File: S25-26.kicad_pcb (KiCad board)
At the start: 6 copper layers, 90 x 90 mm, 159 parts, among them IC1 CMV4000-3E5M0PN, IC10 DS90LV048ATM_NOPB, IC2 MXL86110I-AQB-R, IC3 TPS5430DDAR, IC4 MT29F2G01ABAGDWB-IT_G_TR, IC5 MT29F2G01ABAGDWB-IT_G_TR, IC6 XMC7200D-E272K8384AA, IC7 DS90LV011AHMF_NOPB, IC8 DS90LV048ATM_NOPB, IC9 DS90LV048ATM_NOPB, J1 DC_IN_PADS, J2 Conn_01x06_Pin, J3 Conn_01x04_Pin, J4 RJ45_JXD1-0001NL, J5 Conn_01x04_Pin, Q1 ZXT849K, U1 TPS73601MDBVREP, U2 TPS73601MDBVREP, Y1 DSC1101DM2-012.0000, Y2 DSC1101DM2-125.0000T

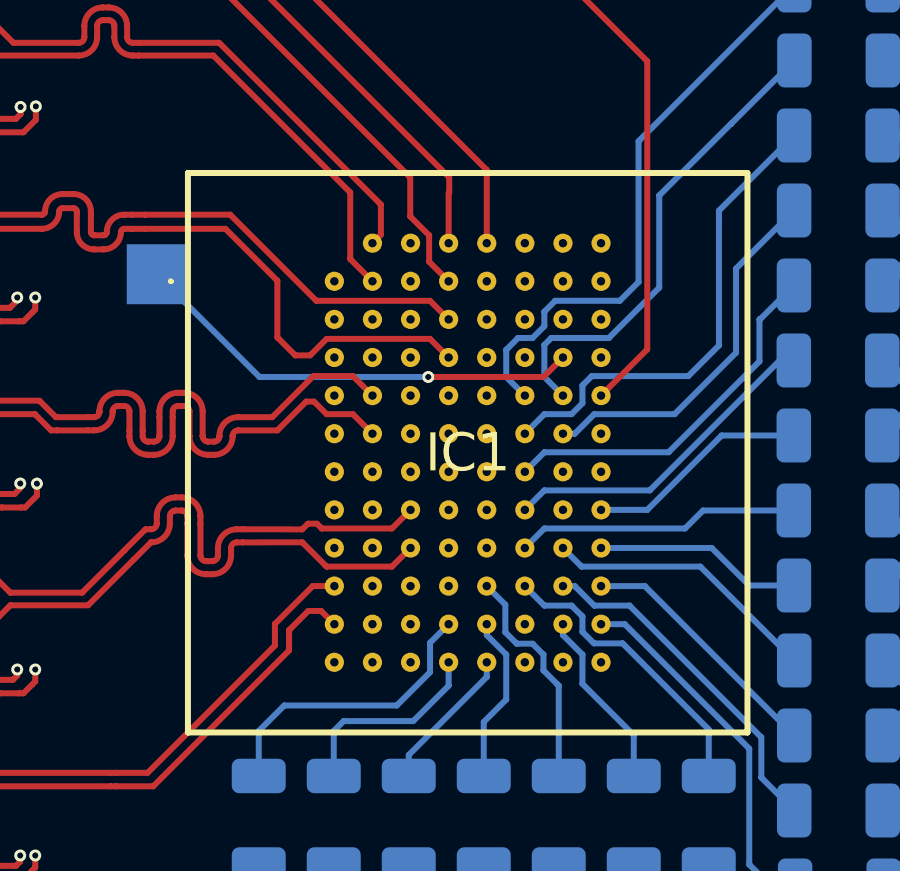
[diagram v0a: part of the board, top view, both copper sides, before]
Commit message: CMOS Sensor Grid Text
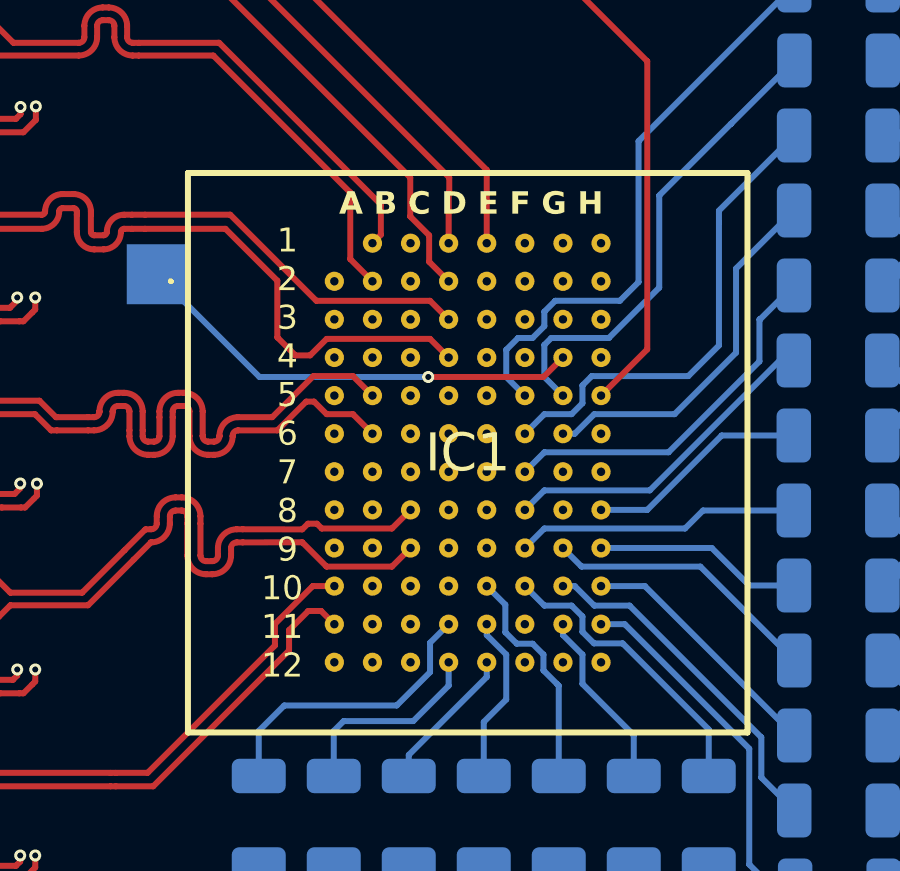
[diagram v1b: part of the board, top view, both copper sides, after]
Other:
- board text added: "1 2 3 4 5 6 7 8 9 10 11 12"
- board text added: "A B C D E F G H"
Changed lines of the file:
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@@
 		(allow_soldermask_bridges_in_footprints no)
 		(tenting front back)
+		(grid_origin 177.5 100)
 		(pcbplotparams
 			(layerselection 0x00000000_00000000_55555555_5755f5ff)
@@
 		)
 	)
+	(gr_text " 1\n 2\n 3\n 4\n 5\n 6\n 7\n 8\n 9\n10\n11\n12"
+		(at 174.23 108.28 0)
+		(layer "F.SilkS")
+		(effects
+			(font
+				(size 0.8 0.8)
+				(thickness 0.15)
+			)
+		)
+	)
 	(gr_text "CTS\n"
 		(at 113.5 106 0)
@@
 			)
 		)
+	)
+	(gr_text "A B C D E F G H"
+		(at 180.53 99.96 0)
+		(layer "F.SilkS")
+		(effects
+			(font
+				(size 0.75 0.75)
+				(thickness 0.15)
+				(bold yes)
+			)
+		)

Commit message: Beginning of V3
Long way to go
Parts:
- added R17: 10k, Resistor_SMD:R_1206_3216Metric, F.Cu at (180.3, 126.3)
- added R18: 10k, Resistor_SMD:R_1206_3216Metric, F.Cu at (180.3, 129.6)
- added R19: 10k, Resistor_SMD:R_1206_3216Metric, F.Cu at (180.3, 132.8)
- IC1: footprint SamacSys_Parts:CMV40003E5M0PN -> CustomFootprintLibrary:CMV40003E5M0PN_Socket
- J2: footprint Connector_PinHeader_2.54mm:PinHeader_1x06_P2.54mm_Vertical -> Connector_PinHeader_1.27mm:PinHeader_2x05_P1.27mm_Vertical_SMD
- J4: footprint Connector_RJ:RJ45_UDE_RB1-125B8G1A -> CustomFootprintLibrary:RJ45_JXD1-0001NL
- Q1: footprint Package_TO_SOT_SMD:TO-252-3_TabPin4 -> CustomFootprintLibrary:TO-252-3_TabPin4
- R6: footprint Resistor_SMD:R_0805_2012Metric -> Resistor_SMD:R_1206_3216Metric
- moved J2 35.3 mm to (186.6, 133.4)
- moved VCORE1 3.48 mm to (169.6, 123.4)
- moved C62 1.45 mm to (171.5, 125.6), turned to 0 degrees
- moved R6 0.71 mm to (166.5, 125.6), turned to 0 degrees
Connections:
- IC6 pad K18: Net-(IC6B-XRES__L) -> /Processing/XRES
- J2 pad 1: /Processing/SWJ_SWCLK_TCLK -> +3V3
- J2 pad 3: /Processing/SWJ_SWO_TDO -> GND
- J2 pad 4: /Processing/SWJ_SWDOE_TDI -> /Processing/SWJ_SWCLK_TCLK
- J2 pad 5: /Processing/SWJ_TRSTN -> GND
- J2 pad 6: GND -> /Processing/SWJ_SWO_TDO
- R14 pad 1: Net-(IC6B-XRES__L) -> /Processing/XRES
- XRES1 pad 1: Net-(IC6B-XRES__L) -> /Processing/XRES
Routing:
- net +3V3: track 566.8 -> 457.7 mm
- net /Processing/SWJ_TRSTN: track 31.5 -> 0.10 mm, vias 2 -> 0
- net Net-(IC6B-XRES__L): track 9.21 -> 0.00 mm, vias 1 -> 0
- net /Processing/XRES: track 0.00 -> 9.21 mm, vias 0 -> 1
- net /Processing/EXT_PS_CTL1: track 80.4 -> 71.5 mm
- added copper zone on F.Cu, net /Processing/EXT_PS_CTL0
- added copper zone on F.Cu, net /Processing/EXT_PS_CTL1

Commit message: Excluded TPs from BOM
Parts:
- removed IC2: MXL86110I-AQB-R, SamacSys_Parts:QFN40P500X500X95-41N-D
- removed R3: 2.49k, Resistor_SMD:R_1206_3216Metric
- removed TP8: VDD1V1, TestPoint:TestPoint_Pad_2.0x2.0mm
- added IC11: DP83867IRPAPT, SamacSys_Parts:QFP50P1200X1200X120-65N, F.Cu at (216.2, 87.0)
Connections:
- net /HRSTN renamed /Processing/HRSTN
- R12 pad 2: Net-(IC2-GPHY_LED0/CFG_EXT) -> unconnected-(R12-Pad2)
- R13 pad 2: Net-(IC2-GPHY_LED1/CFG_LDO0) -> unconnected-(R13-Pad2)
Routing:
- net unconnected-(R12-Pad2): track 0.00 -> 42.0 mm, vias 0 -> 2
- net Net-(IC2-GPHY_LED0/CFG_EXT): track 42.0 -> 0.00 mm, vias 2 -> 0
- net unconnected-(R13-Pad2): track 0.00 -> 37.4 mm, vias 0 -> 2
- net Net-(IC2-GPHY_LED1/CFG_LDO0): track 37.4 -> 0.00 mm, vias 2 -> 0
- net (no net): track 0.00 -> 29.2 mm, vias 0 -> 5
- net /VDD1V1: track 25.4 -> 0.00 mm, vias 5 -> 0
- net Net-(IC2-RCAL): track 3.72 -> 0.00 mm

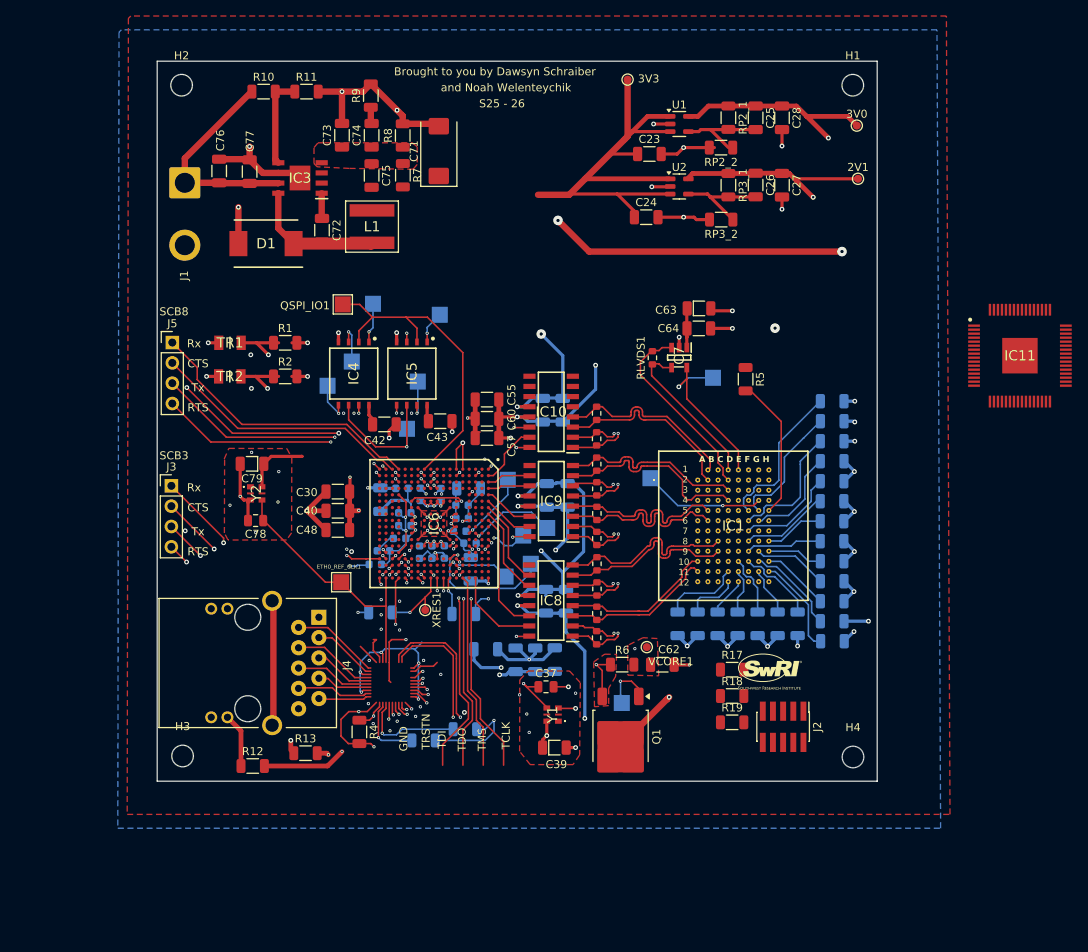
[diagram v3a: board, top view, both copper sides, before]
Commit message: V3 Overhaul
Things remaining:
Ethernet Transceiver Clocks
Output Filtering on DC-DC Converter
Update some part numbers
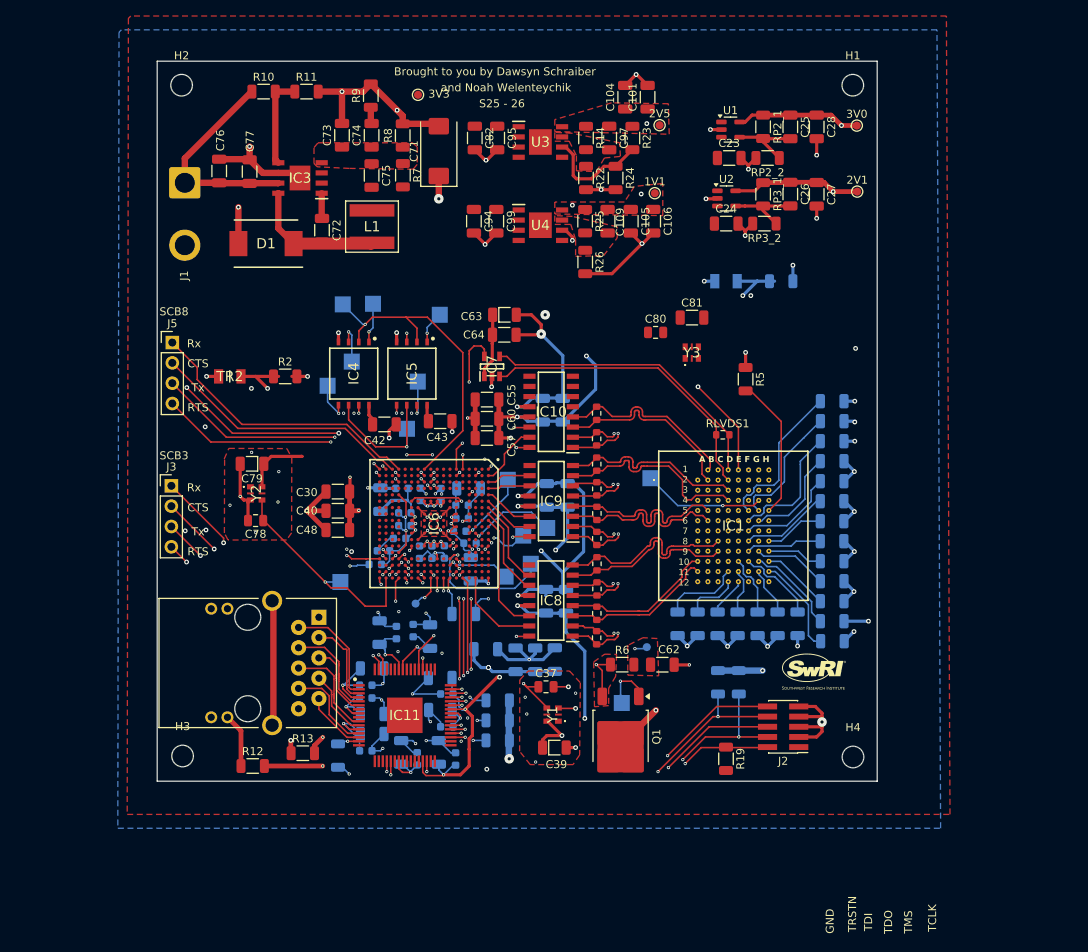
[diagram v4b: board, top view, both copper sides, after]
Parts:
- removed CMOS_MASTER_CLK1: CMOS_MASTER_CLK, TestPoint:TestPoint_Pad_2.0x2.0mm
- added 1V1: TestPoint, TestPoint:TestPoint_Pad_D1.0mm, F.Cu at (170.6, 66.7)
- added 2V5: TestPoint, TestPoint:TestPoint_Pad_D1.0mm, F.Cu at (171.2, 58.2)
- added C100: 1uF, Capacitor_SMD:C_1206_3216Metric, B.Cu at (135.3, 134.3)
- added C101: 0.1uF, Capacitor_SMD:C_1206_3216Metric, F.Cu at (169.7, 54.7)
- added C102: 0.1uF, Capacitor_SMD:C_0603_1608Metric, B.Cu at (134.5, 136.4)
- added C103: 1uF, Capacitor_SMD:C_1206_3216Metric, B.Cu at (142.5, 122.1)
- added C104: 1uF, Capacitor_SMD:C_1206_3216Metric, F.Cu at (166.9, 54.7)
- added C105: 1uF, Capacitor_SMD:C_1206_3216Metric, F.Cu at (167.6, 70.2)
- added C106: 0.1uF, Capacitor_SMD:C_1206_3216Metric, F.Cu at (170.4, 70.2)
- added C109: 0.01uF, Capacitor_SMD:C_1206_3216Metric, F.Cu at (164.7, 70.2)
- added C111: 1uF, Capacitor_SMD:C_1206_3216Metric, B.Cu at (138.9, 136.6)
- added C112: 1uF, Capacitor_SMD:C_1206_3216Metric, B.Cu at (143.8, 131.3)
- added C80: 15pF, Capacitor_SMD:C_0805_2012Metric, F.Cu at (170.7, 84.1)
- added C81: 0.1uF, Capacitor_SMD:C_1206_3216Metric, F.Cu at (175.2, 82.2)
- added C82: 10uF, Capacitor_SMD:C_1206_3216Metric, F.Cu at (148.1, 59.8)
- added C83: 1uF, Capacitor_SMD:C_1206_3216Metric, B.Cu at (143.6, 136.6)
- added C84: 0.1uF, Capacitor_SMD:C_0603_1608Metric, B.Cu at (140.4, 121.4)
- added C85: 0.1uF, Capacitor_SMD:C_0603_1608Metric, B.Cu at (145.7, 137.4)
- added C86: 1uF, Capacitor_SMD:C_1206_3216Metric, B.Cu at (143.8, 127.3)
- added C87: 0.1uF, Capacitor_SMD:C_0603_1608Metric, B.Cu at (144.6, 129.3)
- added C88: 0.1uF, Capacitor_SMD:C_0603_1608Metric, B.Cu at (140.9, 137.4)
- added C89: 1uF, Capacitor_SMD:C_1206_3216Metric, B.Cu at (135.3, 131.8)
- added C90: 0.1uF, Capacitor_SMD:C_0603_1608Metric, B.Cu at (138.3, 121.6)
- added C91: 1uF, Capacitor_SMD:C_1206_3216Metric, B.Cu at (136.2, 121.6)
- added C92: 0.1uF, Capacitor_SMD:C_0603_1608Metric, B.Cu at (144.6, 133.4)
- added C93: 0.1uF, Capacitor_SMD:C_0603_1608Metric, B.Cu at (134.5, 129.8)
- added C94: 10uF, Capacitor_SMD:C_1206_3216Metric, F.Cu at (148.0, 70.2)
- added C95: 0.22uF, Capacitor_SMD:C_1206_3216Metric, F.Cu at (150.9, 59.8)
- added C96: 1uF, Capacitor_SMD:C_1206_3216Metric, B.Cu at (135.3, 126.1)
- added C97: 2200pF, Capacitor_SMD:C_1206_3216Metric, F.Cu at (164.9, 59.8)
- added C98: 0.1uF, Capacitor_SMD:C_0603_1608Metric, B.Cu at (134.5, 128.2)
- added C99: 0.22uF, Capacitor_SMD:C_1206_3216Metric, F.Cu at (150.8, 70.2)
- added R22: 47k, Resistor_SMD:R_1206_3216Metric, F.Cu at (162.0, 64.8)
- added R23: 7.5k, Resistor_SMD:R_1206_3216Metric, F.Cu at (167.8, 59.8)
- added R24: 10k, Resistor_SMD:R_1206_3216Metric, F.Cu at (165.7, 64.8)
- added R25: 4.99k, Resistor_SMD:R_1206_3216Metric, F.Cu at (161.9, 70.2)
- added R26: 13.3k, Resistor_SMD:R_1206_3216Metric, F.Cu at (161.9, 75.3)
- added R3: 11k, Resistor_SMD:R_1206_3216Metric, B.Cu at (131.0, 137.0)
- added U3: TLS208D1EJVXUMA1, SamacSys_Parts:SOIC127P600X170-9N, F.Cu at (156.3, 60.3)
- added U4: TLS208D1EJVXUMA1, SamacSys_Parts:SOIC127P600X170-9N, F.Cu at (156.3, 70.7)
- added Y3: DSC1101DM2-025.0000, SamacSys_Parts:DSC1101DM20120000, F.Cu at (175.2, 86.6)
- ETH0_REF_CLK1, QSPI_IO1, R1, R17, R18, R4, TR1, VCORE1, XRES1: moved to B.Cu
- R14: value 10k -> 100k; moved to F.Cu
- moved IC11 89.1 mm to (139.3, 132.0)
- moved R14 64.6 mm to (162.0, 59.8), turned to -90 degrees
- moved R1 62.5 mm to (186.4, 77.7)
- moved TR1 62.5 mm to (179.5, 77.7)
- moved 3V3 26.3 mm to (141.0, 54.4)
- moved C63 24.3 mm to (151.8, 81.9)
- moved C64 24.3 mm to (151.8, 84.4)
- moved IC7 23.4 mm to (150.2, 88.3), turned to 90 degrees
- moved R4 17.7 mm to (151.0, 130.1), turned to 0 degrees
- moved RLVDS1 13.0 mm to (179.1, 96.9), turned to 180 degrees
- moved C24 10.0 mm to (179.5, 70.5)
- moved C23 9.99 mm to (179.9, 62.3)
- moved R15 9.59 mm to (151.0, 132.6)
- moved U1 6.44 mm to (180.1, 58.8)
- moved U2 6.09 mm to (179.6, 67.3)
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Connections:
- net +3V renamed +3V0
- C78 pad 1: /ETH0_REF_CLK -> /Processing/GTX_CLK
- IC11 pad 12: unconnected-(IC11-VDDA2P5_2-Pad12) -> +2V5
- IC11 pad 15: unconnected-(IC11-RBIAS-Pad15) -> Net-(IC11-RBIAS)
- IC11 pad 19: unconnected-(IC11-X_I-Pad19) -> /Processing/XTAL_IN
- IC11 pad 22: unconnected-(IC11-CLK_OUT-Pad22) -> /Processing/ETH0_REF_CLK (P18.0)
- IC11 pad 23: unconnected-(IC11-VDDIO_1-Pad23) -> +3V3
- IC11 pad 29: unconnected-(IC11-VDD1P1_2-Pad29) -> +1V1
- IC11 pad 4: unconnected-(IC11-VDDA2P5_1-Pad4) -> +2V5
- IC11 pad 40: unconnected-(IC11-GTX_CLK-Pad40) -> /Processing/GTX_CLK
- IC11 pad 41: unconnected-(IC11-VDDIO_2-Pad41) -> +3V3
- IC11 pad 42: unconnected-(IC11-VDD1P1_3-Pad42) -> +1V1
- IC11 pad 57: unconnected-(IC11-VDDIO_3-Pad57) -> +3V3
- IC11 pad 58: unconnected-(IC11-VDD1P1_4-Pad58) -> +1V1
- IC11 pad 62: unconnected-(IC11-LED_1-Pad62) -> Net-(IC11-LED_1)
- IC11 pad 63: unconnected-(IC11-LED_0-Pad63) -> Net-(IC11-LED_0)
- IC11 pad 65: unconnected-(IC11-EP-Pad65) -> GND
- IC11 pad 8: unconnected-(IC11-VDD1P1_1-Pad8) -> +1V1
- IC6 pad E1: /CMOS_MASTER_CLK -> /Processing/CMOS_LVDS_CLK_IN
- IC6 pad U18: /ETH0_REF_CLK -> /Processing/ETH0_REF_CLK (P18.0)
- IC7 pad 5: /CMOS_MASTER_CLK -> /Processing/CMOS_LVDS_CLK_IN
- R12 pad 2: unconnected-(R12-Pad2) -> Net-(IC11-LED_1)
- R13 pad 2: unconnected-(R13-Pad2) -> Net-(IC11-LED_0)
- R14 pad 1: /Processing/XRES -> +2V5
- R14 pad 2: +3V3 -> /Voltage Regulation/ADJ/FB_2V5
- R5 pad 1: +3V3 -> GND
- Y2 pad 4: /ETH0_REF_CLK -> /Processing/GTX_CLK
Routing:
- net +1V1: track 0.00 -> 199.4 mm, vias 0 -> 8
- net +2V5: track 0.00 -> 172.6 mm, vias 0 -> 5
- net +3V3: track 457.7 -> 313.5 mm, vias 35 -> 36
- net GND: track 528.3 -> 433.5 mm, vias 99 -> 101
- net /Processing/XRES: track 9.21 -> 59.2 mm, vias 1 -> 2
- net unconnected-(R12-Pad2): track 42.0 -> 0.00 mm, vias 2 -> 0
- net unconnected-(R13-Pad2): track 37.4 -> 0.00 mm, vias 2 -> 0
- net /Processing/SWJ_SWDOE_TDI: track 26.3 -> 62.7 mm, vias 2 -> 5
- net /Processing/SWJ_SWCLK_TCLK: track 28.2 -> 62.8 mm, vias 2 -> 5
- net /Processing/SWJ_SWO_TDO: track 26.4 -> 59.1 mm, vias 2 -> 4
- net /Processing/TEMPR_ADC0 (P6.0): track 30.0 -> 61.6 mm, vias 2 -> 4
- net /Processing/SWJ_SWDIO_TMS: track 24.5 -> 55.1 mm, vias 0 -> 2
- net (no net): track 29.2 -> 0.00 mm, vias 5 -> 0
- net Net-(IC11-LED_1): track 0.00 -> 26.1 mm, vias 0 -> 2
- net /Processing/CMOS_LVDS_CLK_IN: track 0.00 -> 18.7 mm, vias 0 -> 2
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- added copper zone on F.Cu, net +1V1
- added copper zone on F.Cu, net +2V5
- added copper zone on F.Cu, net /Voltage Regulation/ADJ/FB_1V1
- added copper zone on F.Cu, net /Voltage Regulation/ADJ/FB_2V5

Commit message: Some mild V3 changes
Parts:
- removed ETH0_REF_CLK1: ETH0_REF_CLK, TestPoint:TestPoint_Pad_2.0x2.0mm
- removed R4: 10k, Resistor_SMD:R_1206_3216Metric
- C103, C84, C90, C91, R17, R18, XRES1: moved to F.Cu
- C62, Q1, R6: moved to B.Cu
- moved XRES1 47.7 mm to (93.5, 111.1), turned to 0 degrees
- moved Q1 32.3 mm to (137.2, 120.6), turned to 180 degrees
- moved C62 23.2 mm to (148.7, 121.7)
- moved R6 21.8 mm to (144.9, 122.5), turned to 90 degrees
- moved VCORE1 17.7 mm to (152.0, 121.5)
- moved DRV_VOUT1 12.2 mm to (178.4, 128.0)
- moved R18 8.53 mm to (189.6, 127.1)
- moved R17 7.83 mm to (186.3, 127.2)
- moved C90 3.11 mm to (135.2, 121.3)
- moved C103 2.69 mm to (139.9, 121.4)
- moved C49 1.60 mm to (148.3, 119.2)
- moved C84 1.50 mm to (141.9, 121.4)
- moved C91 1.14 mm to (137.3, 121.3)
- moved C51 0.60 mm to (149.5, 124.3)
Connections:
- C78 pad 1: /Processing/GTX_CLK -> /Processing/ETH0_REF_CLK (P18.0)
- IC11 pad 22: /Processing/ETH0_REF_CLK (P18.0) -> unconnected-(IC11-CLK_OUT-Pad22)
- IC11 pad 40: /Processing/GTX_CLK -> /Processing/ETH0_REF_CLK (P18.0)
- IC6 pad E1: /Processing/CMOS_LVDS_CLK_IN -> unconnected-(IC6B-P7.0-PadE1)
- IC6 pad J3: unconnected-(IC6B-P24.0-PadJ3) -> /Processing/CMOS_LVDS_CLK_IN
- IC6 pad M17: unconnected-(IC6B-P21.2-PadM17) -> /Processing/ECO_IN
- IC6 pad M18: /Processing/ECO_IN -> unconnected-(IC6B-P21.3-PadM18)
- Y2 pad 4: /Processing/GTX_CLK -> /Processing/ETH0_REF_CLK (P18.0)
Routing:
- net /Processing/ETH0_REF_CLK (P18.0): track 0.00 -> 48.4 mm
- net /Processing/DRV_VOUT: track 35.6 -> 4.06 mm, vias 2 -> 1
- net /ETH0_REF_CLK: track 27.9 -> 0.00 mm, vias 1 -> 0
- net GND: track 433.5 -> 405.8 mm, vias 101 -> 100
- net /Processing/EXT_PS_CTL0: track 30.7 -> 12.9 mm, vias 2 -> 1
- net /Processing/EXT_PS_CTL1: track 73.0 -> 55.7 mm, vias 6 -> 4
- net /ETH0_TXD_3: track 31.8 -> 35.9 mm
- net /Processing/SWJ_SWCLK_TCLK: track 62.8 -> 66.7 mm, vias 5 -> 4
- net /Processing/HRSTN: track 21.8 -> 19.6 mm
- net /Processing/XRES: track 59.2 -> 57.1 mm
- net /ETH0_TXD_1: track 29.7 -> 27.9 mm
- net /Processing/SWJ_SWDOE_TDI: track 62.7 -> 64.3 mm, vias 5 -> 4
- net /ETH0_TXD_0: track 33.8 -> 34.8 mm
- net /ETH0_RX_CLK: track 21.0 -> 22.0 mm
- net +3V3: track 313.5 -> 314.3 mm, vias 36 -> 39
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- added copper zone on In2.Cu, net +3V3
- added copper zone on In4.Cu, net +3V3
- removed copper zone on F.Cu, net /Processing/EXT_PS_CTL0
- removed copper zone on F.Cu, net /Processing/EXT_PS_CTL1
